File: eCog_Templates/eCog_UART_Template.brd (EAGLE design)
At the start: 47.5 x 28 mm, 11 parts

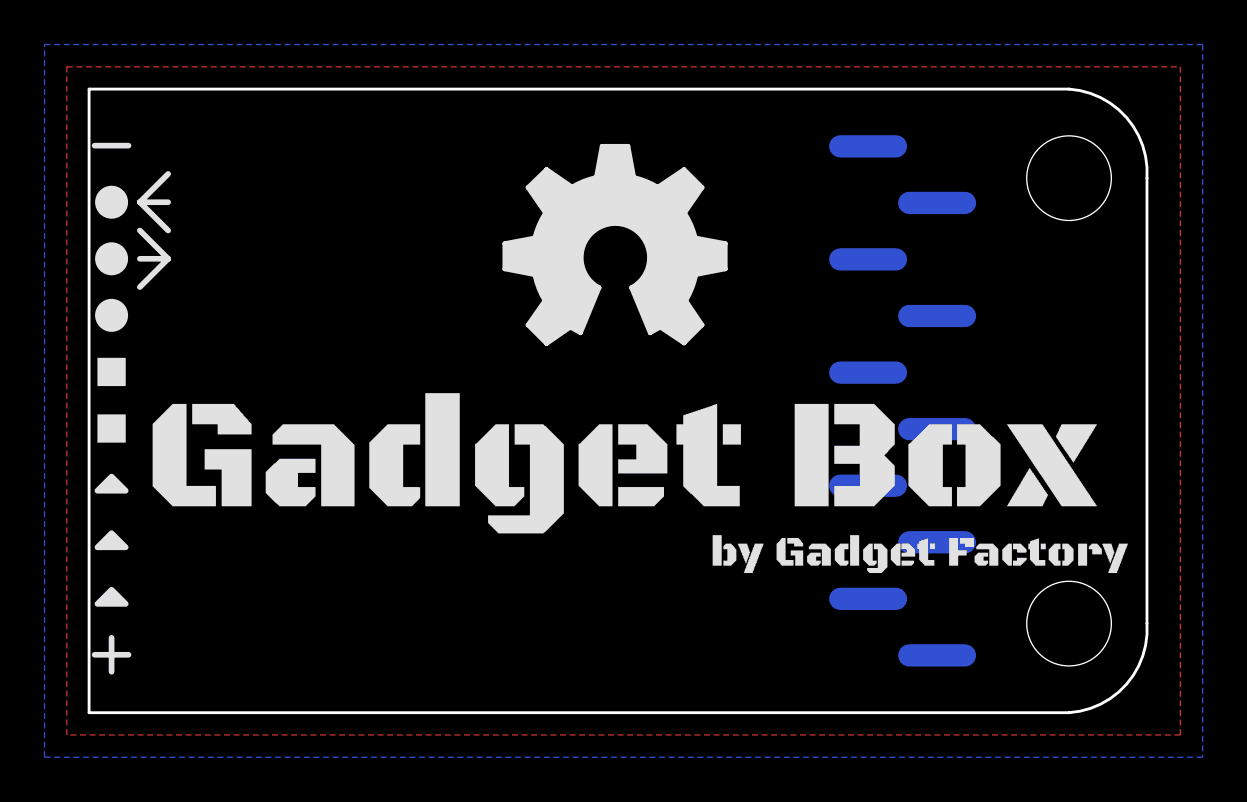
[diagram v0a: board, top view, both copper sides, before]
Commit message: Change to through hole and give bette descriptions.
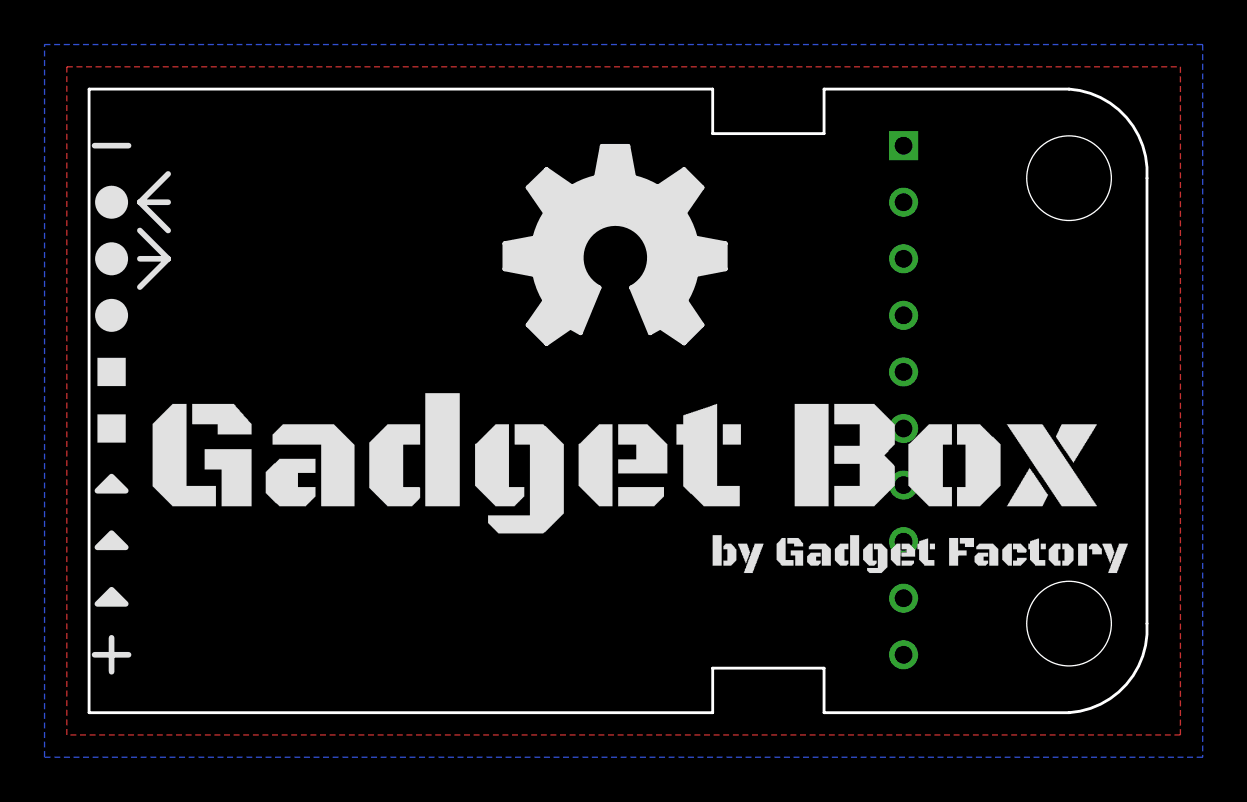
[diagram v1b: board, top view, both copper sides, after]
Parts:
- ECOG: value ECOG_GENERAL_ROWECOG_GENERAL_SMD -> ECOG_GENERAL_ROWTHROUGHOLE; device eCogs:ECOG_GENERAL_SMD -> eCogs:ECOG_GENERAL_TH
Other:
- outline, holes or cut-outs redrawn
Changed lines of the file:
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@@
 </autorouter>
 <elements>
-<element name="ECOG" library="eCogs" package="ECOG_GENERAL_SMD" value="ECOG_GENERAL_ROWECOG_GENERAL_SMD" x="48.26" y="27.94" smashed="yes" rot="R180">
-<attribute name="DIGIKEY" value="S1013EC-10-ND" x="48.26" y="27.94" size="1.778" layer="27" rot="R180" display="off"/>
-</element>
+<element name="ECOG" library="eCogs" package="ECOG_GENERAL_TH" value="ECOG_GENERAL_ROWTHROUGHOLE" x="48.26" y="27.94" smashed="yes" rot="R180"/>
 <element name="U$2" library="eCogs" package="LEGEND_DIO" value="" x="1.27" y="22.86"/>
 <element name="U$3" library="eCogs" package="LEGEND_DIO" value="" x="1.27" y="20.32"/>
